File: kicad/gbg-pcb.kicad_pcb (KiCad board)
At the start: 2 copper layers, 99.1 x 99.1 mm, 74 parts, among them J1 1017514, J2 Screw_Terminal_01x04, J3 Screw_Terminal_01x03, J4 1017514, J5 VP0265840000G, J6 Conn_01x09_Pin, J7 Conn_01x02, Q1 SQD40031EL_GE3, Q2 SQD40031EL_GE3, Q3 SQD40031EL_GE3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

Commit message: move traces
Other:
- board text added: "15 14 GND 13 12 11 10 GND 9 8 7 6 B6 GND 5 B5 4 B4 3 B3 2 B2 GND 1 B1 0"
- board text added: "28 A"
- board text added: "LED"
- board text removed: "15 14 GND 13 led 12 11 10 GND 9 8 7 6 B6 GND 5 B5 4 B4 3 B3 2 B2 GND 1 B1 0"
- board text removed: "28"
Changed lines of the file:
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@@
 		)
 		(property "Value" "rpi pico"
-			(at -2.413 -4.318 90)
+			(at 0.0038 0.85 180)
 			(layer "F.SilkS")
 			(effects
@@
 		(tags "THT Terminal Block Phoenix MKDS-1,5-3-5.08 pitch 5.08mm size 15.2x9.8mm^2 drill 1.3mm pad 2.6mm")
 		(property "Reference" "J3"
-			(at 13.721 1.727 90)
+			(at 13.721 1.727 180)
 			(layer "F.SilkS")
 			(effects
@@
 		(tags "C Radial series Radial pin pitch 5.00mm diameter 10mm height 16mm Non-Polar Electrolytic Capacitor")
 		(property "Reference" "C2"
-			(at 6.35 -5.207 0)
+			(at -1.773 4.74 0)
 			(layer "F.SilkS")
 			(effects
@@
 			)
 		)
-		(property "Description" ""
+		(property "Description" "screw terminal 65A"
 			(at 0 0 90)
 			(layer "F.Fab")
@@
 		)
 	)
-	(gr_text "28"
-		(at 133.223 138.684 90)
+	(gr_text "28\nA"
+		(at 135.751 137.133 90)
 		(layer "F.SilkS")
 		(effects
@@
 				(bold yes)
 			)
-			(justify left bottom)
+			(justify bottom)
 		)
 	)
@@
 		)
 	)
-	(gr_text "15\n14\nGND\n13 led\n12\n11\n10\nGND\n9\n8\n7\n6 B6\nGND\n5 B5\n4 B4\n3 B3\n2 B2\nGND\n1 B1\n0"
+	(gr_text "LED"
+		(at 112.751 102.133 0)
+		(layer "B.SilkS")
+		(effects
+			(font
+				(size 1 1)
+				(thickness 0.1)
+			)
+			(justify left bottom mirror)
+		)
+	)
+	(gr_text "15\n14\nGND\n13\n12\n11\n10\nGND\n9\n8\n7\n6 B6\nGND\n5 B5\n4 B4\n3 B3\n2 B2\nGND\n1 B1\n0"
 		(at 116.251 143.133 0)
 		(layer "B.SilkS")
@@
 	)
 	(segment
-		(start 95.758 100.838)
-		(end 96.393 101.473)
+		(start 94.827906 84.646174)
+		(end 94.827906 84.858406)
 		(width 0.2032)
 		(layer "F.Cu")
@@
 	)
 	(segment
+		(start 96.393 101.473)
+		(end 98.2218 101.473)
+		(width 0.2032)
+		(layer "F.Cu")
+		(net 11)
+	)
+	(segment
 		(start 93.345 76.454)
 		(end 94.742 77.851)
@@
 	)
 	(segment
-		(start 94.742 77.851)
-		(end 94.742 82.423)
+		(start 94.827906 84.858406)
+		(end 95.758 85.7885)
 		(width 0.2032)
 		(layer "F.Cu")
@@
 	)
 	(segment
-		(start 92.837 76.454)
-		(end 93.345 76.454)
+		(start 94.742 77.851)
+		(end 94.742 82.423)
 		(width 0.2032)
 		(layer "F.Cu")
@@
 	)
 	(segment
-		(start 96.393 101.473)
-		(end 98.2218 101.473)
+		(start 92.837 76.454)
+		(end 93.345 76.454)
 		(width 0.2032)
 		(layer "F.Cu")
@@
 	)
 	(segment
-		(start 94.742 84.7725)
-		(end 95.758 85.7885)
+		(start 95.758 100.838)
+		(end 96.393 101.473)
 		(width 0.2032)
 		(layer "F.Cu")
@@
 	)
 	(via
-		(at 94.742 84.7725)
+		(at 94.827906 84.646174)
 		(size 0.6)
 		(drill 0.3)
@@
 	)
 	(segment
-		(start 94.869 84.836)
-		(end 94.869 82.55)
+		(start 94.827906 84.646174)
+		(end 94.868326 84.646174)
+		(width 0.2032)
+		(layer "B.Cu")
+		(net 11)
+	)
+	(segment
+		(start 94.827906 84.646174)
+		(end 94.869 84.60508)
 		(width 0.2032)
 		(layer "B.Cu")
@@
 	)
 	(segment
-		(start 94.742 84.7725)
+		(start 94.869 84.60508)
+		(end 94.869 82.55)
+		(width 0.2032)
+		(layer "B.Cu")
+		(net 11)
+	)
+	(segment
+		(start 94.868326 84.646174)
 		(end 94.869 84.6455)
 		(width 0.2032)
@@
 	)
 	(segment
-		(start 95.631 84.7725)
-		(end 96.266 85.4075)
+		(start 96.266 85.4075)
+		(end 96.266 95.943964)
 		(width 0.2032)
 		(layer "F.Cu")
@@
 	)
 	(segment
-		(start 96.266 85.4075)
-		(end 96.266 95.943964)
-		(width 0.2032)
-		(layer "F.Cu")
-		(net 20)
-	)
-	(segment
 		(start 57.531 76.073)
 		(end 57.912 75.692)
@@
 	)
 	(segment
-		(start 75.311 77.978)
-		(end 75.311 80.1646)
+		(start 96.715036 96.393)
+		(end 98.2218 96.393)
 		(width 0.2032)
 		(layer "F.Cu")
@@
 	)
 	(segment
-		(start 96.715036 96.393)
-		(end 98.2218 96.393)
+		(start 75.311 77.978)
+		(end 75.311 80.1646)
 		(width 0.2032)
 		(layer "F.Cu")
@@
 	)
 	(segment
-		(start 96.266 95.943964)
-		(end 96.715036 96.393)
+		(start 76.2 77.089)
+		(end 75.311 77.978)
 		(width 0.2032)
 		(layer "F.Cu")
@@
 	)
 	(segment
-		(start 76.2 77.089)
-		(end 75.311 77.978)
+		(start 95.631 84.633)
+		(end 95.631 84.7725)
+		(width 0.2032)
+		(layer "F.Cu")
+		(net 20)
+	)
+	(segment
+		(start 95.631 84.7725)
+		(end 96.266 85.4075)
 		(width 0.2032)
 		(layer "F.Cu")
@@
 	)
 	(segment
+		(start 96.266 95.943964)
+		(end 96.715036 96.393)
+		(width 0.2032)
+		(layer "F.Cu")
+		(net 20)
+	)
+	(segment
 		(start 93.599 75.819)
 		(end 95.504 77.724)
@@
 	)
 	(via
-		(at 95.631 84.7725)
+		(at 95.631 84.633)
 		(size 0.6)
 		(drill 0.3)
@@
 	)
 	(segment
-		(start 76.2 77.089)
-		(end 76.2 76.708)
+		(start 95.631 82.423)
+		(end 95.631 84.633)
 		(width 0.2032)
 		(layer "B.Cu")
@@
 	)
 	(segment
-		(start 76.2 76.708)
-		(end 75.438 75.946)
+		(start 76.2 77.089)
+		(end 76.2 76.708)
 		(width 0.2032)
 		(layer "B.Cu")
@@
 	)
 	(segment
-		(start 95.631 82.423)
-		(end 95.631 84.963)
+		(start 76.2 76.708)
+		(end 75.438 75.946)
 		(width 0.2032)
 		(layer "B.Cu")
@@
 	)
 	(segment
+		(start 96.774 91.694)
+		(end 98.2218 93.1418)
+		(width 0.2032)
+		(layer "F.Cu")
+		(net 21)
+	)
+	(segment
 		(start 96.266 77.597)
 		(end 96.266 82.169)
@@
 	)
 	(segment
-		(start 57.658 75.184)
-		(end 85.852 75.184)
+		(start 96.434094 84.686594)
+		(end 96.774 85.0265)
 		(width 0.2032)
 		(layer "F.Cu")
@@
 	)
 	(segment
-		(start 96.774 91.694)
-		(end 98.2218 93.1418)
+		(start 57.658 75.184)
+		(end 85.852 75.184)
 		(width 0.2032)
 		(layer "F.Cu")
@@
 	)
 	(segment
-		(start 96.52 84.7725)
-		(end 96.774 85.0265)
+		(start 96.434094 84.646174)
+		(end 96.434094 84.686594)
 		(width 0.2032)
 		(layer "F.Cu")
@@
 	)
 	(segment
-		(start 98.2218 93.1418)
-		(end 98.2218 93.853)
+		(start 56.261 76.581)
+		(end 57.658 75.184)
 		(width 0.2032)
 		(layer "F.Cu")
@@
 	)
 	(segment
-		(start 56.261 76.581)
-		(end 57.658 75.184)
+		(start 98.2218 93.1418)
+		(end 98.2218 93.853)
 		(width 0.2032)
 		(layer "F.Cu")
@@
 	)
 	(via
-		(at 96.52 84.7725)
+		(at 96.434094 84.646174)
 		(size 0.6)
 		(drill 0.3)
@@
 	)
 	(segment
-		(start 96.52 84.7725)
+		(start 96.393674 84.646174)
 		(end 96.393 84.6455)
 		(width 0.2032)
@@
 	)
 	(segment
-		(start 96.393 82.55)
-		(end 96.52 82.423)
+		(start 96.434094 84.646174)
+		(end 96.393 84.60508)
 		(width 0.2032)
 		(layer "B.Cu")
@@
 	)
 	(segment
-		(start 96.393 84.836)
+		(start 96.393 84.60508)
 		(end 96.393 82.55)
 		(width 0.2032)
@@
 	)
 	(segment
+		(start 96.393 82.55)
+		(end 96.52 82.423)
+		(width 0.2032)
+		(layer "B.Cu")
+		(net 21)
+	)
+	(segment
+		(start 96.434094 84.646174)
+		(end 96.393674 84.646174)
+		(width 0.2032)
+		(layer "B.Cu")
+		(net 21)
+	)
+	(segment
 		(start 79.7328 77.978)
 		(end 84.201 77.978)
@@
 		(polygon
 			(pts
-				(xy 61.214 93.085001) (xy 44.323 93.085001) (xy 44.323 106.68) (xy 61.341 106.68)
+				(xy 61.212582 92.585001) (xy 44.323 92.585001) (xy 44.323 108.633) (xy 61.251 106.133)
 			)
 		)

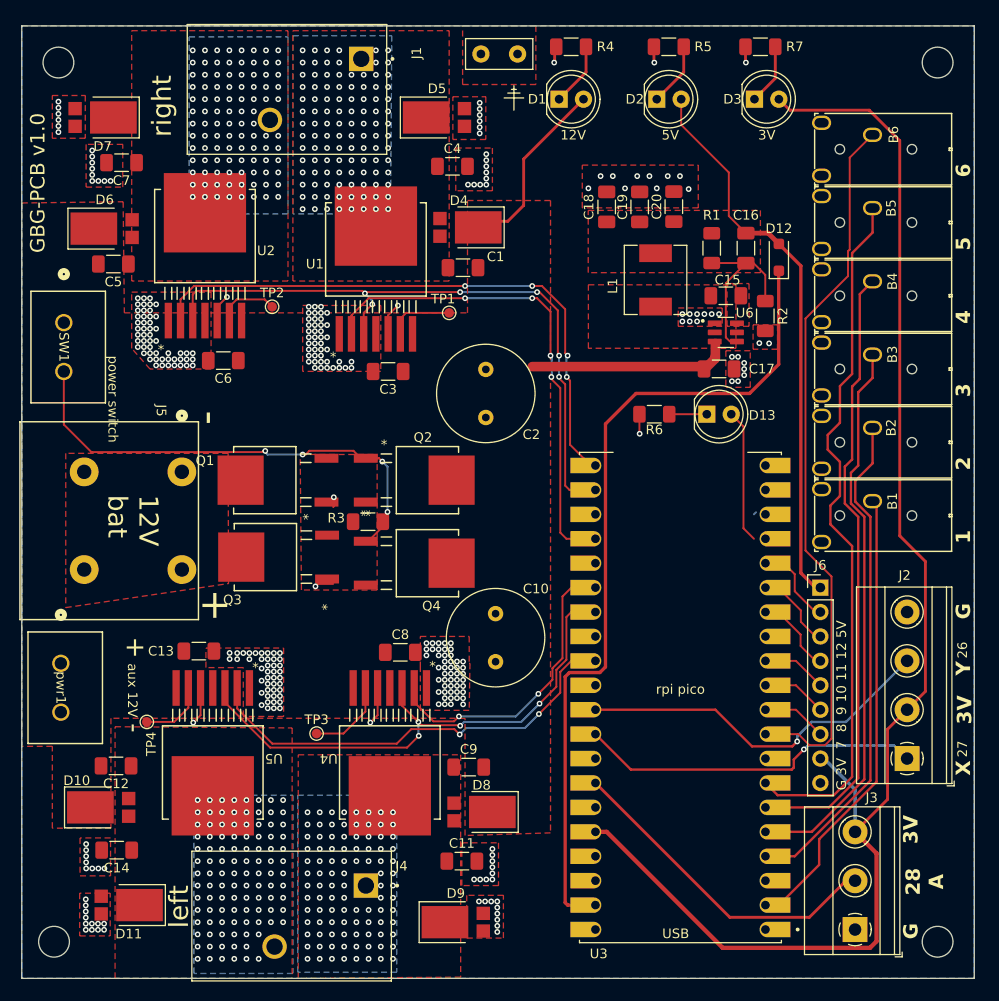
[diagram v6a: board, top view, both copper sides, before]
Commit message: adjust trace width and ground vias
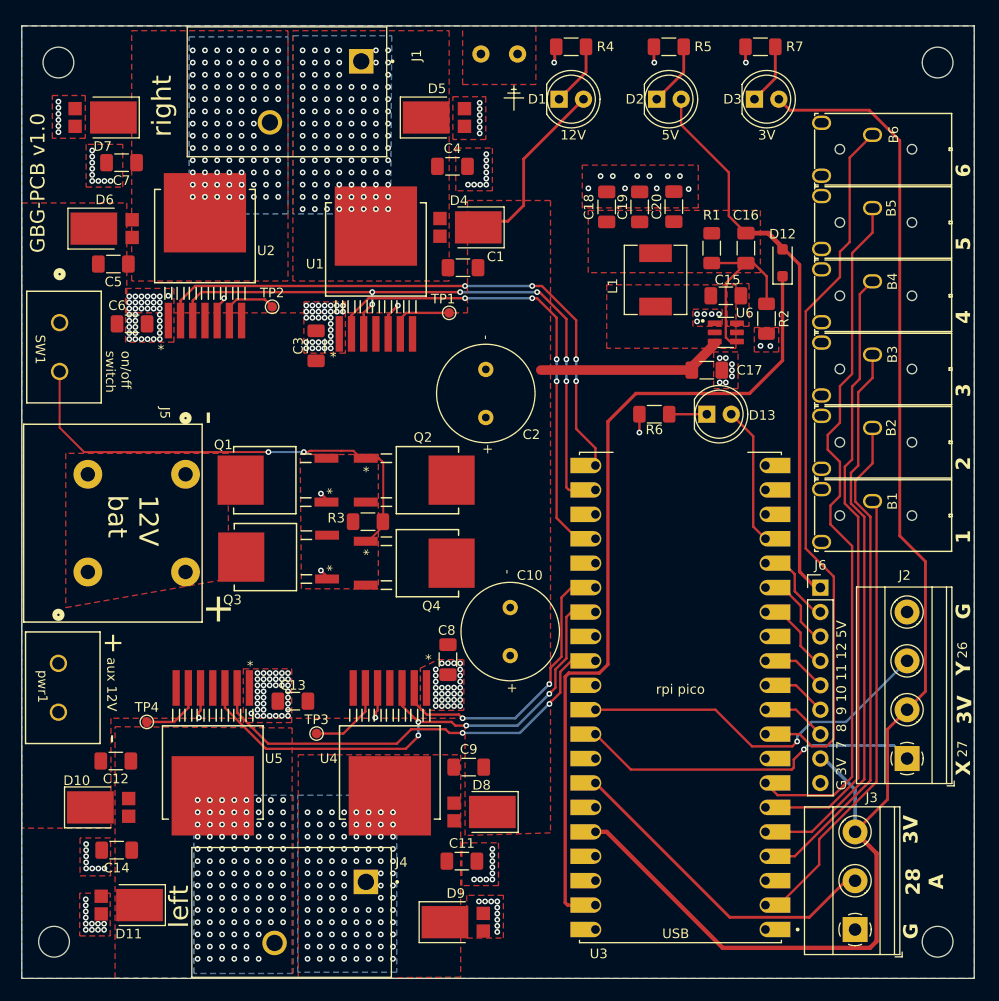
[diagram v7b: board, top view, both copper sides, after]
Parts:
- moved C13 11.1 mm to (67.9, 118.4), turned to 180 degrees
- moved C6 10.2 mm to (51.2, 79.1), turned to 0 degrees
- moved C3 7.95 mm to (70.4, 81.4), turned to 90 degrees
- moved C8 5.01 mm to (84.1, 114.0), turned to -90 degrees
- moved C10 4.62 mm to (90.6, 113.6), turned to 90 degrees
- moved C17 1.28 mm to (111.0, 83.9)
- moved D12 0.68 mm to (118.9, 72.8)
- moved C12 0.51 mm to (49.5, 124.6)
- moved J5 0.46 mm to (56.8, 94.8)
- moved SW1 0.44 mm to (43.7, 79.0)
- moved J4 0.38 mm to (57.4, 133.6)
- moved R2 0.31 mm to (117.2, 78.6)
- moved J1 0.25 mm to (57.0, 48.2)
- moved pwr1 0.25 mm to (43.6, 114.4)
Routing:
- net GND: track 25.4 -> 22.5 mm, vias 296 -> 238
- net +BATT: track 41.1 -> 39.1 mm
- net right_1: track 50.2 -> 49.4 mm
- net right_en: track 67.4 -> 66.6 mm
- net Net-(Q2-G): vias 4 -> 2
- net Net-(D6-A): vias 100 -> 98
- net Net-(D4-A): vias 108 -> 105
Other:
- board text added: "on/off switch"
- board text removed: "power switch"

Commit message: add readme
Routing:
- net +BATT: track 39.1 -> 40.0 mm
- net Net-(D8-A): vias 98 -> 116
- net Net-(D10-A): vias 105 -> 116
